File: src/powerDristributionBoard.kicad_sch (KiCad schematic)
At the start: 15 parts

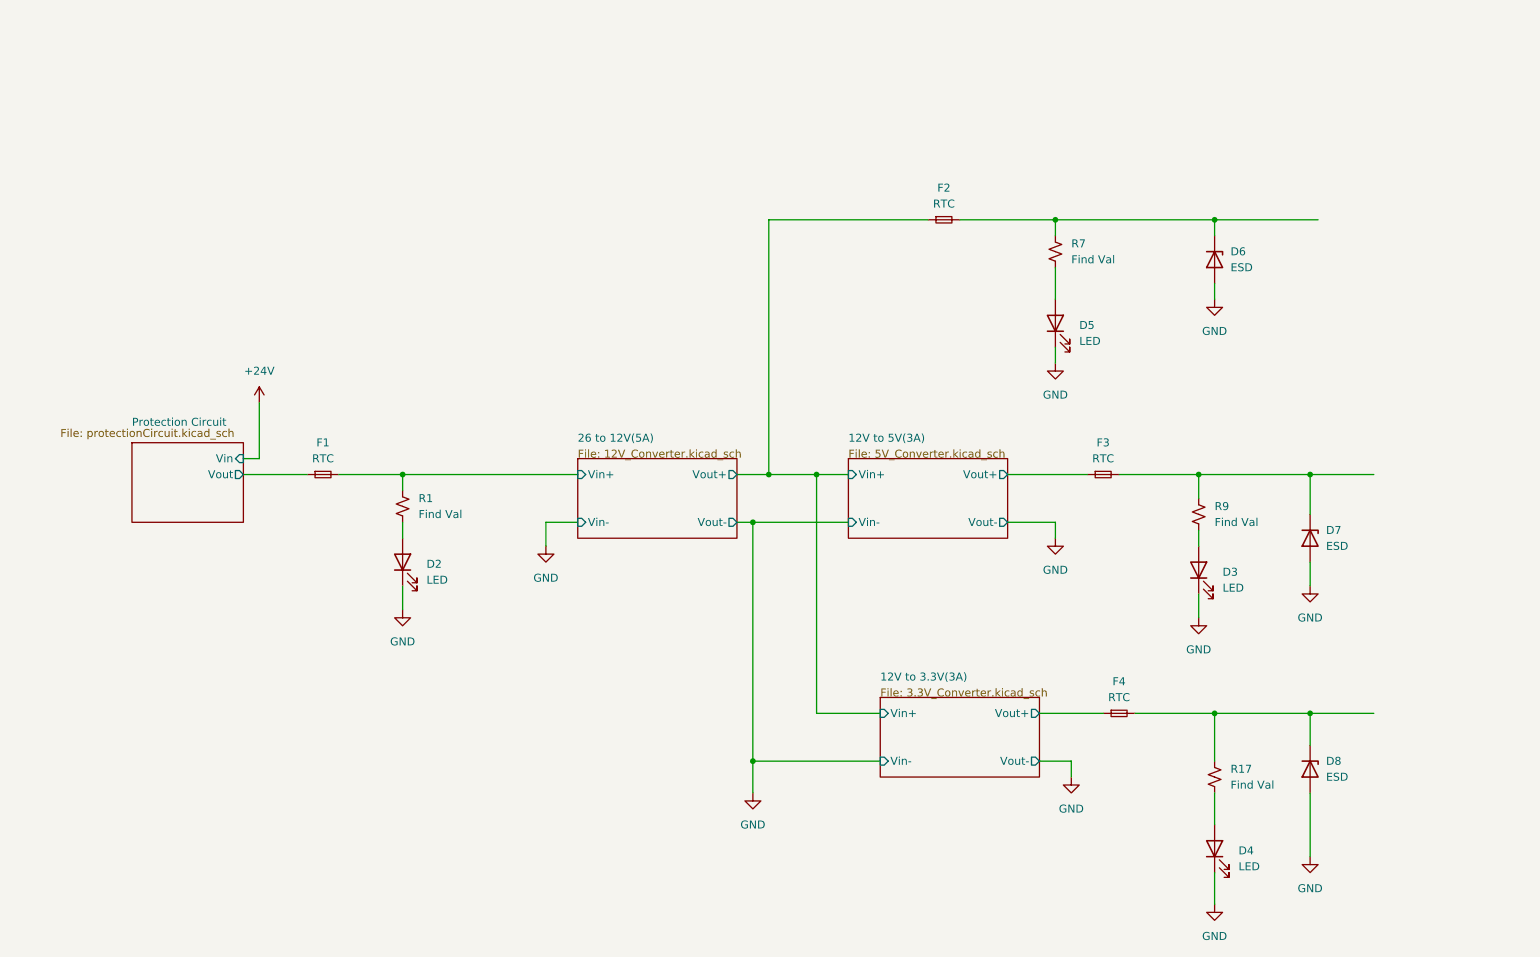
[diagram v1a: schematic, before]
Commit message: Added more components
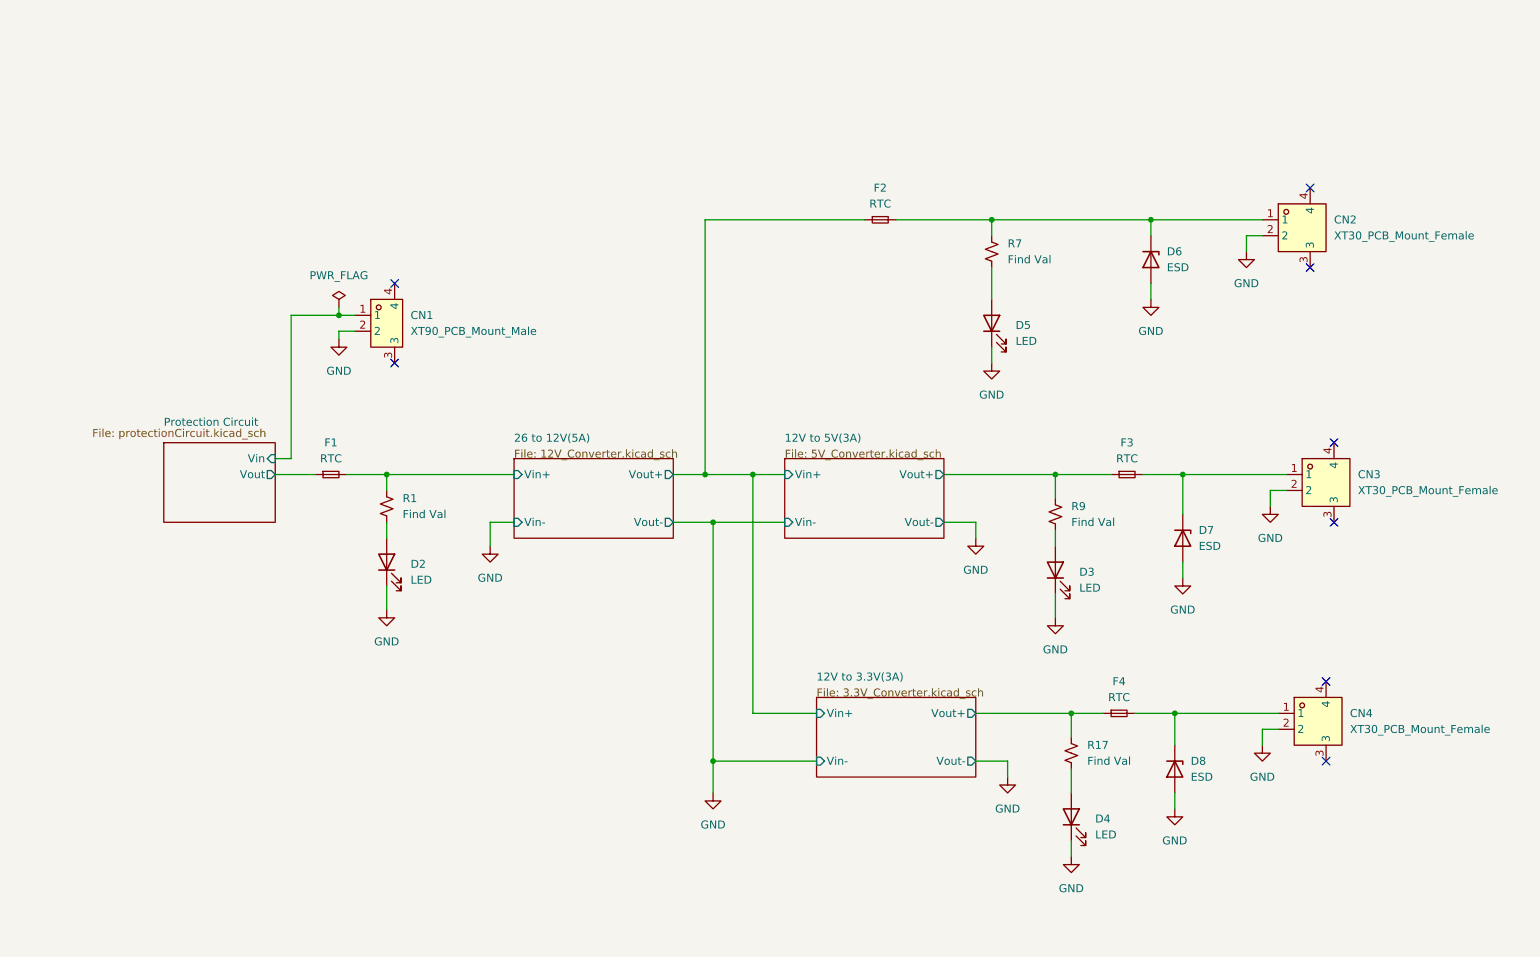
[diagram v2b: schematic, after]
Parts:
- added CN1: XT90_PCB_Mount_Male, PowerPCB_Footprints:XT-90_PCB_Mount_Male, symbol PowerPCB_Symbols:XT90_PCB_Mount_Male
- added CN2, CN3, CN4: XT30_PCB_Mount_Female, PowerPCB_Footprints:XT30_PCB_Mount_Female, symbol PowerPCB_Symbols:XT30_PCB_Mount_Female
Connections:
- net 12V to 3.3V(3A)/Vout+: now also R17.1
- net 12V to 5V(3A)/Vout+: now also R9.1
- net GND: now also CN1.2, CN2.2, CN3.2, CN4.2
- net at D6.1 (K), F2.2, R7.1: now also CN2.1
- net at D7.1 (K), F3.2: now also CN3.1; no longer R9.1
- net at D8.1 (K), F4.2: now also CN4.1; no longer R17.1
- new net Protection Circuit/Vin: CN1.1
- no-connect marks 0 -> 8
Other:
- moved on the sheet: D2, D3, D4, D5, D6, D7, D8, F1, F2, R1, R17, R7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

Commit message: Redesigned 5V regulator and edited libraries
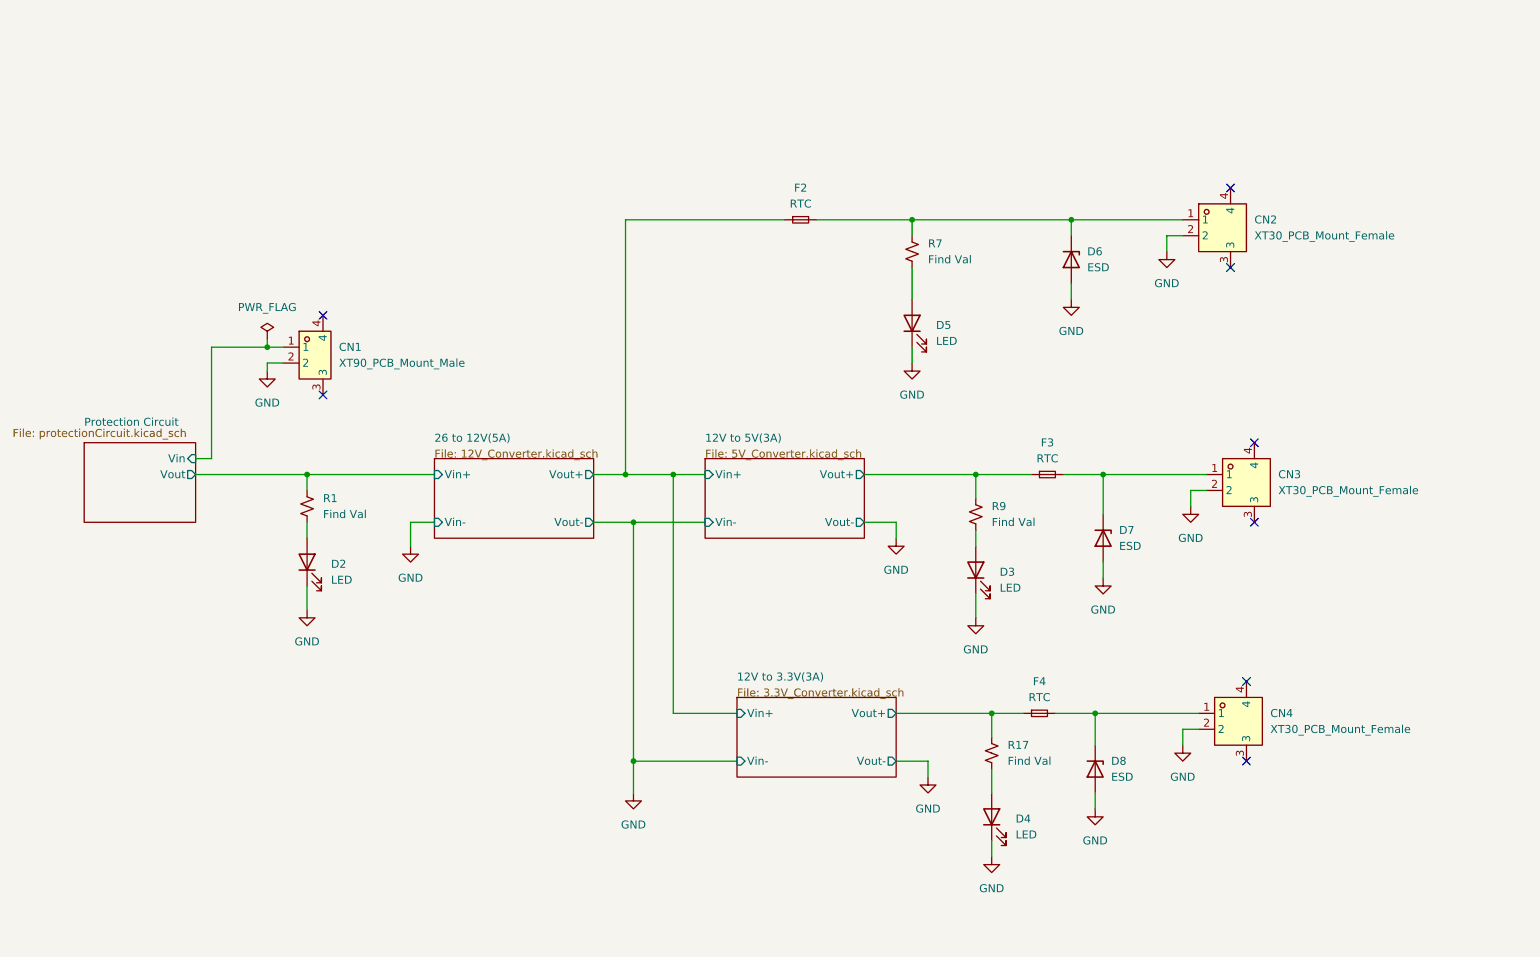
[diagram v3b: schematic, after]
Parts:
- removed F1: RTC, symbol Device:Fuse_Small
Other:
- moved on the sheet: CN1, CN2, CN3, CN4, D2, D3, D4, D5, D6, D7, D8, F2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

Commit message: Added more footprints
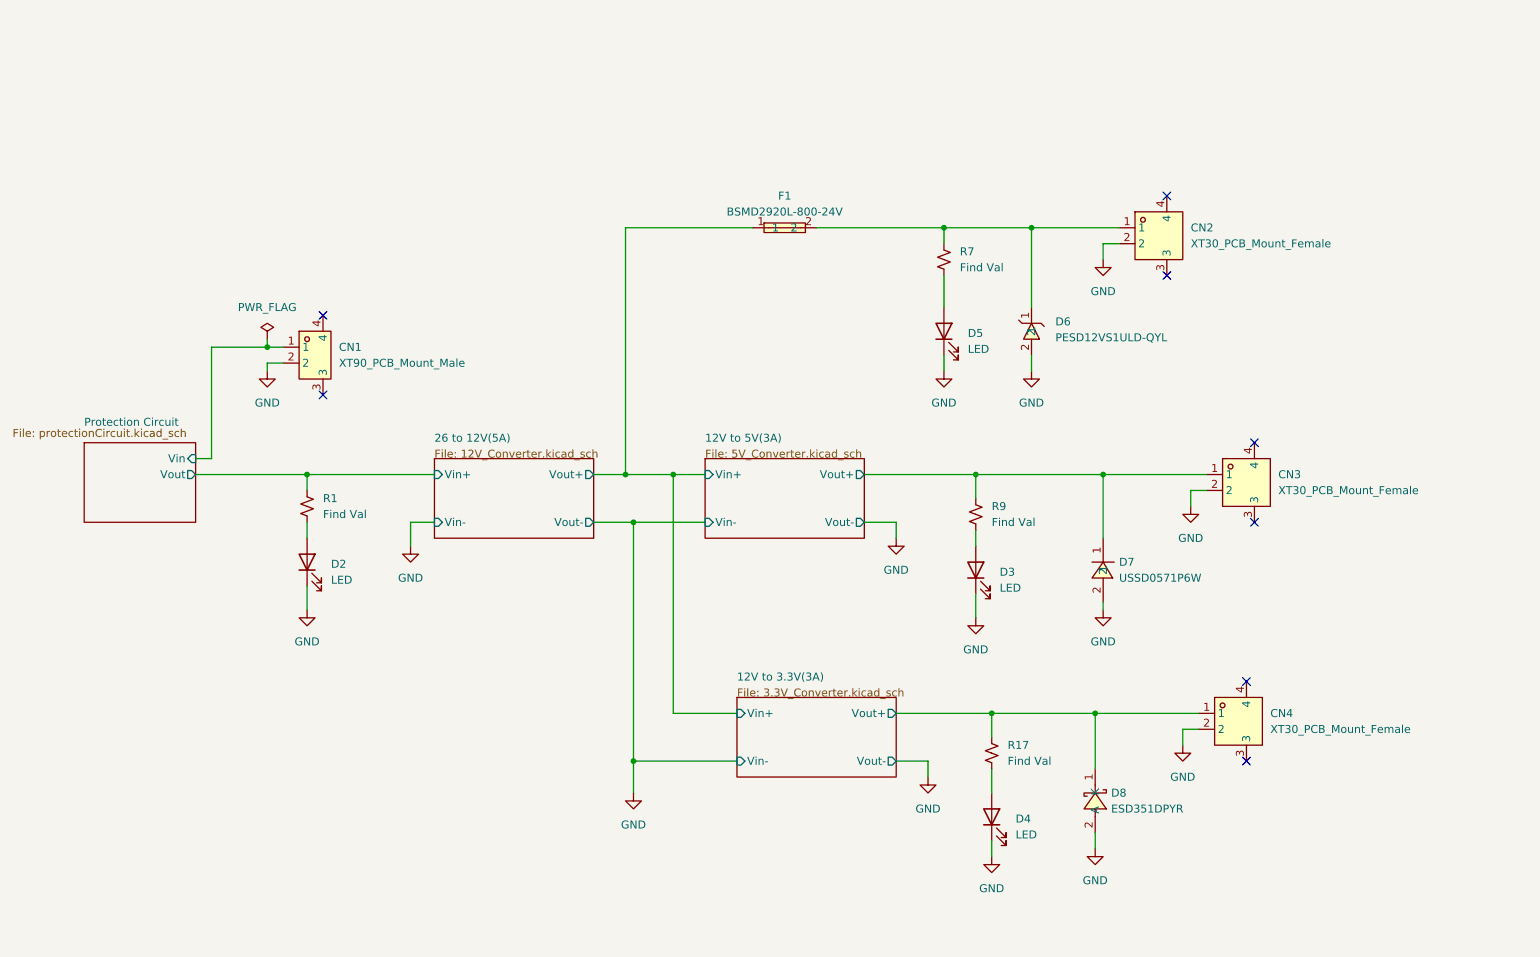
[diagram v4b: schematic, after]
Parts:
- removed D6, D7, D8: ESD, symbol Device:D_Zener
- removed F2, F3, F4: RTC, symbol Device:Fuse_Small
- added D6: PESD12VS1ULD-QYL, PowerPCB_Footprints:PESD12VS1ULD-QYL, symbol PowerPCB_Symbols:PESD12VS1ULD-QYL
- added D7: USSD0571P6W, PowerPCB_Footprints:USSD0571P6W, symbol PowerPCB_Symbols:USSD0571P6W
- added D8: ESD351DPYR, PowerPCB_Footprints:ESD351DPYR, symbol PowerPCB_Symbols:ESD351DPYR
- added F1: BSMD2920L-800-24V, PowerPCB_Footprints:BSMD2920L-800-24V, symbol PowerPCB_Symbols:BSMD2920L-800-24V
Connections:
- net 12V to 3.3V(3A)/Vin+: now also F1.1
- net 12V to 3.3V(3A)/Vout+: now also CN4.1, D8.1 (K)
- net 12V to 5V(3A)/Vout+: now also CN3.1, D7.1
- net GND: now also D6.2, D7.2, D8.2 (A)
- net at CN2.1, R7.1: now also D6.1, F1.2
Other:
- moved on the sheet: CN2, D5, R7

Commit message: Finalized schematic
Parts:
- removed D4: LED, symbol Device:LED
- added D9: LED(Red), LED_SMD:LED_0603_1608Metric, symbol Device:LED
- D2: footprint (none) -> LED_SMD:LED_1206_3216Metric
- D3, D5: footprint (none) -> LED_SMD:LED_0603_1608Metric; now not fitted
- R1: value Find Val -> 22k 0.25W; footprint (none) -> Resistor_SMD:R_1206_3216Metric
- R17, R7, R9: footprint (none) -> Resistor_SMD:R_0603_1608Metric; now not fitted
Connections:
- net GND: now also D9.1 (K)
- net at R17.2: now also D9.2 (A)

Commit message: Edited PCB layout
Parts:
- renumbered CN4 to CN3, CN3 to CN4, D5 to D3, D3 to D4, D9 to D5, D8 to D7, D7 to D8, R1 to R16, R7 to R19, R9 to R20, R17 to R21
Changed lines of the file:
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@@
 		(dnp no)
 		(fields_autoplaced yes)
-		(property "Reference" "#PWR038"
+		(property "Reference" "#PWR036"
 			(at 209.55 140.97 0)
 			(hide yes)
@@
 			(project "powerDristributionBoard"
 				(path "/501e9f3f-9bfa-47dd-b56d-5fd6974f0d03"
-					(reference "#PWR038")
+					(reference "#PWR036")
 					(unit 1)
 				)
@@
 		(dnp no)
 		(fields_autoplaced yes)
-		(property "Reference" "#PWR025"
+		(property "Reference" "#PWR026"
 			(at 121.92 146.05 0)
 			(hide yes)
@@
 			(project "powerDristributionBoard"
 				(path "/501e9f3f-9bfa-47dd-b56d-5fd6974f0d03"
-					(reference "#PWR025")
+					(reference "#PWR026")
 					(unit 1)
 				)
@@
 		(dnp no)
 		(fields_autoplaced yes)
-		(property "Reference" "#PWR01"
+		(property "Reference" "#PWR023"
 			(at 69.85 119.38 0)
 			(hide yes)
@@
 			(project "powerDristributionBoard"
 				(path "/501e9f3f-9bfa-47dd-b56d-5fd6974f0d03"
-					(reference "#PWR01")
+					(reference "#PWR023")
 					(unit 1)
 				)
@@
 		(dnp no)
 		(fields_autoplaced yes)
-		(property "Reference" "#PWR02"
+		(property "Reference" "#PWR022"
 			(at 63.5 81.28 0)
 			(hide yes)
@@
 			(project "powerDristributionBoard"
 				(path "/501e9f3f-9bfa-47dd-b56d-5fd6974f0d03"
-					(reference "#PWR02")
+					(reference "#PWR022")
 					(unit 1)
 				)
@@
 		(dnp no)
 		(fields_autoplaced yes)
-		(property "Reference" "#PWR020"
+		(property "Reference" "#PWR030"
 			(at 176.53 120.65 0)
 			(hide yes)
@@
 			(project "powerDristributionBoard"
 				(path "/501e9f3f-9bfa-47dd-b56d-5fd6974f0d03"
-					(reference "#PWR020")
+					(reference "#PWR030")
 					(unit 1)
 				)
@@
 		(dnp no)
 		(fields_autoplaced yes)
-		(property "Reference" "D7"
+		(property "Reference" "D8"
 			(at 199.39 105.4099 90)
 			(show_name no)
@@
 			(project "powerDristributionBoard"
 				(path "/501e9f3f-9bfa-47dd-b56d-5fd6974f0d03"
-					(reference "D7")
+					(reference "D8")
 					(unit 1)
 				)
@@
 		(dnp no)
 		(fields_autoplaced yes)
-		(property "Reference" "D8"
+		(property "Reference" "D7"
 			(at 198.12 142.2399 90)
 			(show_name no)
@@
 			(project "powerDristributionBoard"
 				(path "/501e9f3f-9bfa-47dd-b56d-5fd6974f0d03"
-					(reference "D8")
+					(reference "D7")
 					(unit 1)
 				)
@@
 		(dnp no)
 		(fields_autoplaced yes)
-		(property "Reference" "#PWR015"
+		(property "Reference" "#PWR024"
 			(at 86.36 109.22 0)
 			(hide yes)
@@
 			(project "powerDristributionBoard"
 				(path "/501e9f3f-9bfa-47dd-b56d-5fd6974f0d03"
-					(reference "#PWR015")
+					(reference "#PWR024")
 					(unit 1)
 				)
@@
 		(dnp no)
 		(fields_autoplaced yes)
-		(property "Reference" "R1"
+		(property "Reference" "R16"
 			(at 72.39 95.2499 0)
 			(show_name no)
@@
 			(project "powerDristributionBoard"
 				(path "/501e9f3f-9bfa-47dd-b56d-5fd6974f0d03"
-					(reference "R1")
+					(reference "R16")
 					(unit 1)
 				)
@@
 		(dnp no)
 		(fields_autoplaced yes)
-		(property "Reference" "#PWR022"
+		(property "Reference" "#PWR028"
 			(at 168.91 146.05 0)
 			(hide yes)
@@
 			(project "powerDristributionBoard"
 				(path "/501e9f3f-9bfa-47dd-b56d-5fd6974f0d03"
-					(reference "#PWR022")
+					(reference "#PWR028")
 					(unit 1)
 				)
@@
 		(dnp yes)
 		(fields_autoplaced yes)
-		(property "Reference" "R9"
+		(property "Reference" "R20"
 			(at 179.07 96.5199 0)
 			(show_name no)
@@
 			(project "powerDristributionBoard"
 				(path "/501e9f3f-9bfa-47dd-b56d-5fd6974f0d03"
-					(reference "R9")
+					(reference "R20")
 					(unit 1)
 				)
@@
 		(dnp no)
 		(fields_autoplaced yes)
-		(property "Reference" "#PWR019"
+		(property "Reference" "#PWR027"
 			(at 163.83 107.95 0)
 			(hide yes)
@@
 			(project "powerDristributionBoard"
 				(path "/501e9f3f-9bfa-47dd-b56d-5fd6974f0d03"
-					(reference "#PWR019")
+					(reference "#PWR027")
 					(unit 1)
 				)
@@
 		(dnp yes)
 		(fields_autoplaced yes)
-		(property "Reference" "D5"
+		(property "Reference" "D3"
 			(at 175.26 68.8974 90)
 			(show_name no)
@@
 			(project "powerDristributionBoard"
 				(path "/501e9f3f-9bfa-47dd-b56d-5fd6974f0d03"
-					(reference "D5")
+					(reference "D3")
 					(unit 1)
 				)
@@
 		(dnp no)
 		(fields_autoplaced yes)
-		(property "Reference" "#PWR021"
+		(property "Reference" "#PWR035"
 			(at 196.85 119.38 0)
 			(hide yes)
@@
 			(project "powerDristributionBoard"
 				(path "/501e9f3f-9bfa-47dd-b56d-5fd6974f0d03"
-					(reference "#PWR021")
+					(reference "#PWR035")
 					(unit 1)
 				)
@@
 		(dnp yes)
 		(fields_autoplaced yes)
-		(property "Reference" "R7"
+		(property "Reference" "R19"
 			(at 173.99 55.8799 0)
 			(show_name no)
@@
 			(project "powerDristributionBoard"
 				(path "/501e9f3f-9bfa-47dd-b56d-5fd6974f0d03"
-					(reference "R7")
+					(reference "R19")
 					(unit 1)
 				)
@@
 		(dnp no)
 		(fields_autoplaced yes)
-		(property "Reference" "#PWR017"
+		(property "Reference" "#PWR029"
 			(at 171.45 81.28 0)
 			(hide yes)
@@
 			(project "powerDristributionBoard"
 				(path "/501e9f3f-9bfa-47dd-b56d-5fd6974f0d03"
-					(reference "#PWR017")
+					(reference "#PWR029")
 					(unit 1)
 				)
@@
 		(dnp no)
 		(fields_autoplaced yes)
-		(property "Reference" "#FLG01"
+		(property "Reference" "#FLG06"
 			(at 63.5 67.945 0)
 			(hide yes)
@@
 			(project "powerDristributionBoard"
 				(path "/501e9f3f-9bfa-47dd-b56d-5fd6974f0d03"
-					(reference "#FLG01")
+					(reference "#FLG06")
 					(unit 1)
 				)
@@
 		(dnp yes)
 		(fields_autoplaced yes)
-		(property "Reference" "D9"
+		(property "Reference" "D5"
 			(at 182.88 146.3674 90)
 			(show_name no)
@@
 			(project "powerDristributionBoard"
 				(path "/501e9f3f-9bfa-47dd-b56d-5fd6974f0d03"
-					(reference "D9")
+					(reference "D5")
 					(unit 1)
 				)
@@
 		(dnp no)
 		(fields_autoplaced yes)
-		(property "Reference" "#PWR018"
+		(property "Reference" "#PWR032"
 			(at 185.42 81.28 0)
 			(hide yes)
@@
 			(project "powerDristributionBoard"
 				(path "/501e9f3f-9bfa-47dd-b56d-5fd6974f0d03"
-					(reference "#PWR018")
+					(reference "#PWR032")
 					(unit 1)
 				)
@@
 		(dnp no)
 		(fields_autoplaced yes)
-		(property "Reference" "CN3"
+		(property "Reference" "CN4"
 			(at 224.79 91.4399 0)
 			(show_name no)
@@
 			(project "powerDristributionBoard"
 				(path "/501e9f3f-9bfa-47dd-b56d-5fd6974f0d03"
-					(reference "CN3")
+					(reference "CN4")
 					(unit 1)
 				)
@@
 		(dnp no)
 		(fields_autoplaced yes)
-		(property "Reference" "#PWR023"
+		(property "Reference" "#PWR031"
 			(at 179.07 158.75 0)
 			(hide yes)
@@
 			(project "powerDristributionBoard"
 				(path "/501e9f3f-9bfa-47dd-b56d-5fd6974f0d03"
-					(reference "#PWR023")
+					(reference "#PWR031")
 					(unit 1)
 				)
@@
 		(dnp yes)
 		(fields_autoplaced yes)
-		(property "Reference" "D3"
+		(property "Reference" "D4"
 			(at 180.34 106.9974 90)
 			(show_name no)
@@
 			(project "powerDristributionBoard"
 				(path "/501e9f3f-9bfa-47dd-b56d-5fd6974f0d03"
-					(reference "D3")
+					(reference "D4")
 					(unit 1)
 				)
@@
 		(dnp yes)
 		(fields_autoplaced yes)
-		(property "Reference" "R17"
+		(property "Reference" "R21"
 			(at 181.61 134.6199 0)
 			(show_name no)
@@
 			(project "powerDristributionBoard"
 				(path "/501e9f3f-9bfa-47dd-b56d-5fd6974f0d03"
-					(reference "R17")
+					(reference "R21")
 					(unit 1)
 				)
@@
 		(dnp no)
 		(fields_autoplaced yes)
-		(property "Reference" "CN4"
+		(property "Reference" "CN3"
 			(at 223.52 129.5399 0)
 			(show_name no)
@@
 			(project "powerDristributionBoard"
 				(path "/501e9f3f-9bfa-47dd-b56d-5fd6974f0d03"
-					(reference "CN4")
+					(reference "CN3")
 					(unit 1)
 				)
@@
 		(dnp no)
 		(fields_autoplaced yes)
-		(property "Reference" "#PWR024"
+		(property "Reference" "#PWR033"
 			(at 195.58 157.48 0)
 			(hide yes)
@@
 			(project "powerDristributionBoard"
 				(path "/501e9f3f-9bfa-47dd-b56d-5fd6974f0d03"
-					(reference "#PWR024")
-					(unit 1)
-				)
+					(reference "#PWR033")
+					(unit 1)
+				)

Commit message: GG
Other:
- moved on the sheet: CN1, CN2, CN3, CN4, D2, D3, D4, D5, D6, D7, D8, F1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
